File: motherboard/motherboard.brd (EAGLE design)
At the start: 105.1 x 137.2 mm, 55 parts, among them IC1 USB6B1, Q1 MOSFET-NCHANNELPTH2, T1 2N3904, T2 2N3904, U1 LED_100V_BUCK, U2 LED_100V_BUCK, U3 LED_100V_BUCK, U4 LED_100V_BUCK, X1 USB_3P-85-32003-00X-1

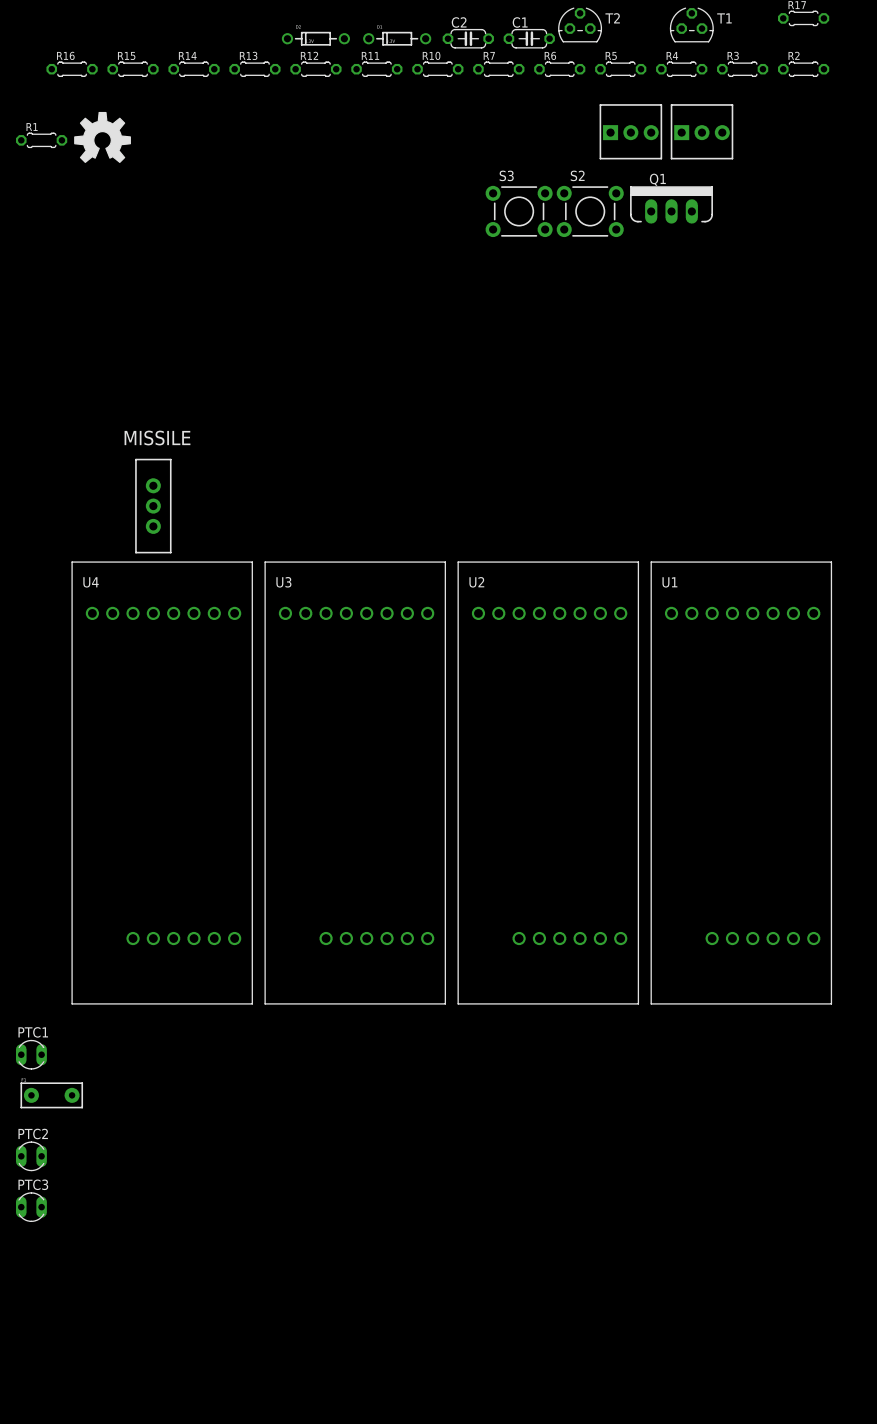
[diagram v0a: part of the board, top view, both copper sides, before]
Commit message: Add under voltage cutoff to LED drivers
Add exports of the motherboard schematic.
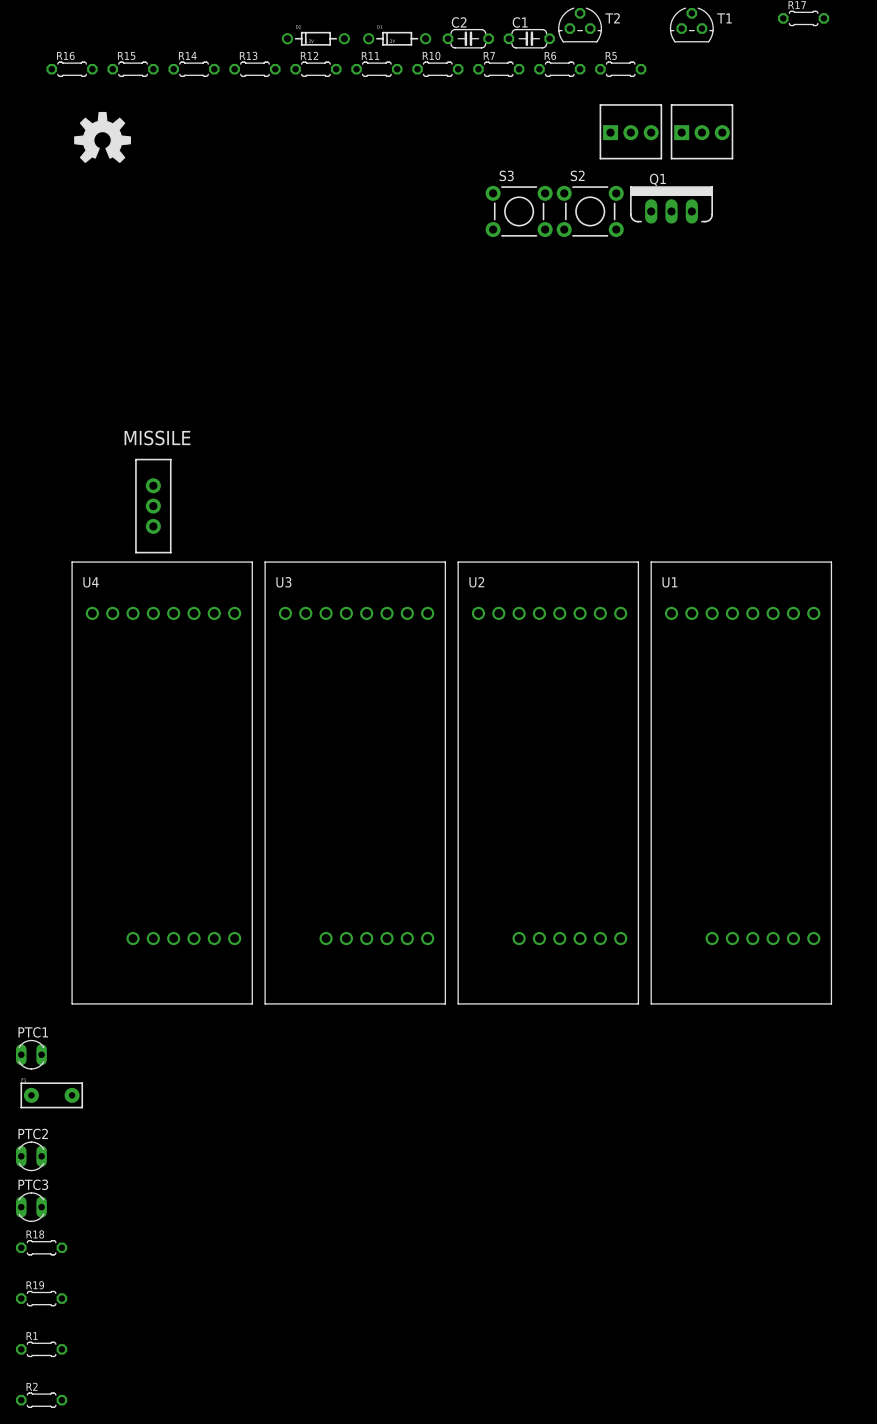
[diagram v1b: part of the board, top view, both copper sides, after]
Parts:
- removed R3, R4: 10k, rcl:0204/5
- added R18: 1M, rcl:0204/5
- added R19: 36k, rcl:0204/5
- R1: value 10k -> 1M
- R2: value 10k -> 25k
- moved R2 191.7 mm to (-111.8, -48.3)
- moved R1 151.1 mm to (-111.8, -41.9)
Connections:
- removed net N$12: R4.1, U4.JL1
- removed net N$13: R2.1, U2.JL1
- net +5V: no longer R1.2, R2.2, R3.2, R4.2
- net GND: now also R19.1, R2.1
- net N$10: now also R2.2, U2.JL1
- net N$11: now also R18.1, R19.2, U4.JL1; no longer R3.1
- net V+: now also R1.2, R18.2

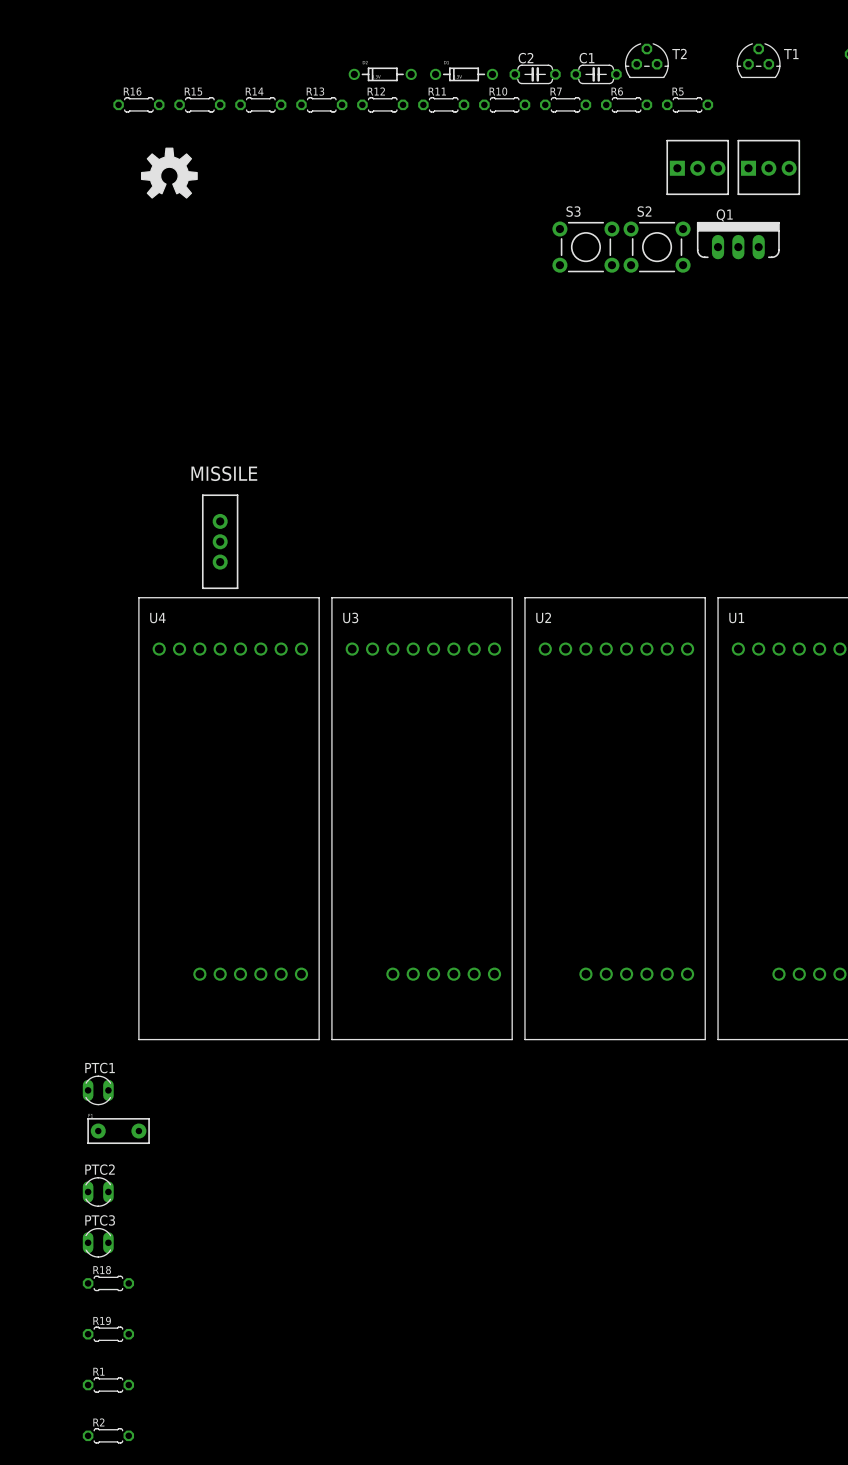
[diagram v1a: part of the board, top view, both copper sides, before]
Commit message: Add LTC2990 current and voltage monitoring chip
Still needs to be connected.
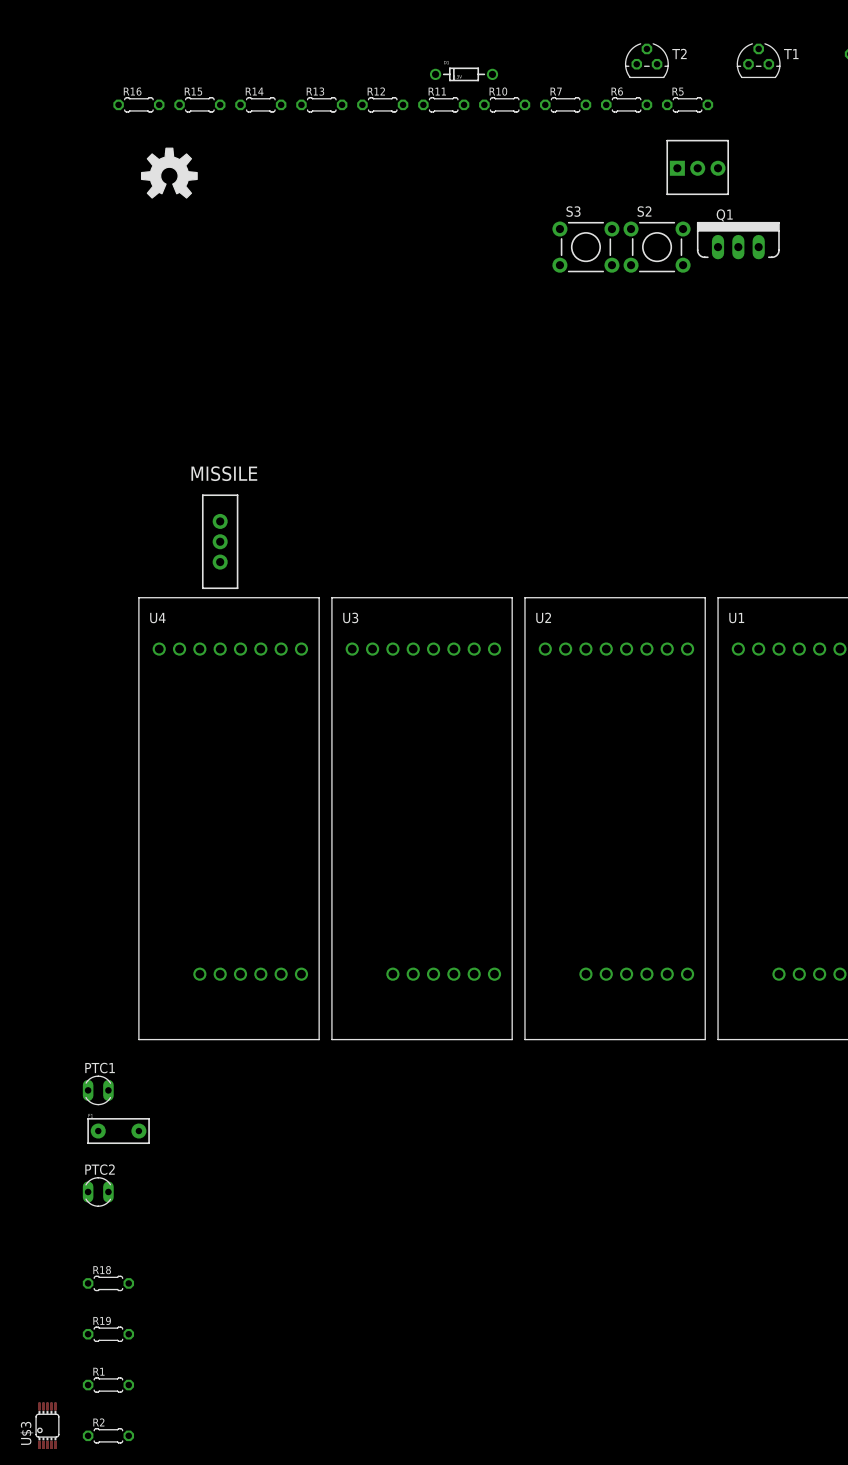
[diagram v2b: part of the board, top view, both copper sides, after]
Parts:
- removed C1, C2: (no value), rcl:C050-024X044
- removed D2: 3.3V, SparkFun-DiscreteSemi:DIODE-ZENER
- removed PTC3: (no value), ptc-ntc:P679
- removed R8: 100k, SparkFun-Electromechanical:3362U-2
- added U$3: LTC2990, droidcycle:MSOP10
- R13, R14: value 1k -> 10k
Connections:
- removed net MOT_CUR: D2.P$1, OA1.1, R8.3, U$1.15
- removed net N$21: F1.P$2, R11.1
- removed net N$22: C2.1, PHOTO.2, R13.2
- removed net N$23: C1.1, PHOTO.4, R14.2
- removed net N$27: PTC3.2, X1.2-1
- removed net VCC: IC1.1
- new net N$12: R6.1
- new net N$13: IC1.2, X1.1-2
- new net V-: OA1.4
- net +3V3: now also R13.1, R14.1
- net +5V: now also IC1.1; no longer OA1.8, PTC3.1
- net BATT_SENSE: no longer U$1.16
- net CADENCE: now also U$1.8
- net GND: no longer C1.2, C2.2, D2.P$2, OA1.4, X1.2-4
- net N$16: now also IC1.3, X1.1-3; no longer OA1.2, R6.1, R8.2
- net N$17: no longer OA1.3
- net PHOTO1: now also PHOTO.4, R14.2, U$1.15; no longer R14.1
- net PHOTO2: now also PHOTO.2, R13.2, U$1.16; no longer R13.1
- net SPEED: now also U$1.7
- net V+: now also F1.P$2, OA1.8, R11.1
